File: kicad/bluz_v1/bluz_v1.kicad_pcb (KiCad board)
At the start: 2 copper layers, 24.9 x 14.9 mm, 61 parts, among them J1 USB_B_Micro, J10 Conn, J11 Conn, J12 BTAnt, J2 Conn, J3 Conn, J4 Conn, J5 Conn, J6 Conn, J7 Conn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

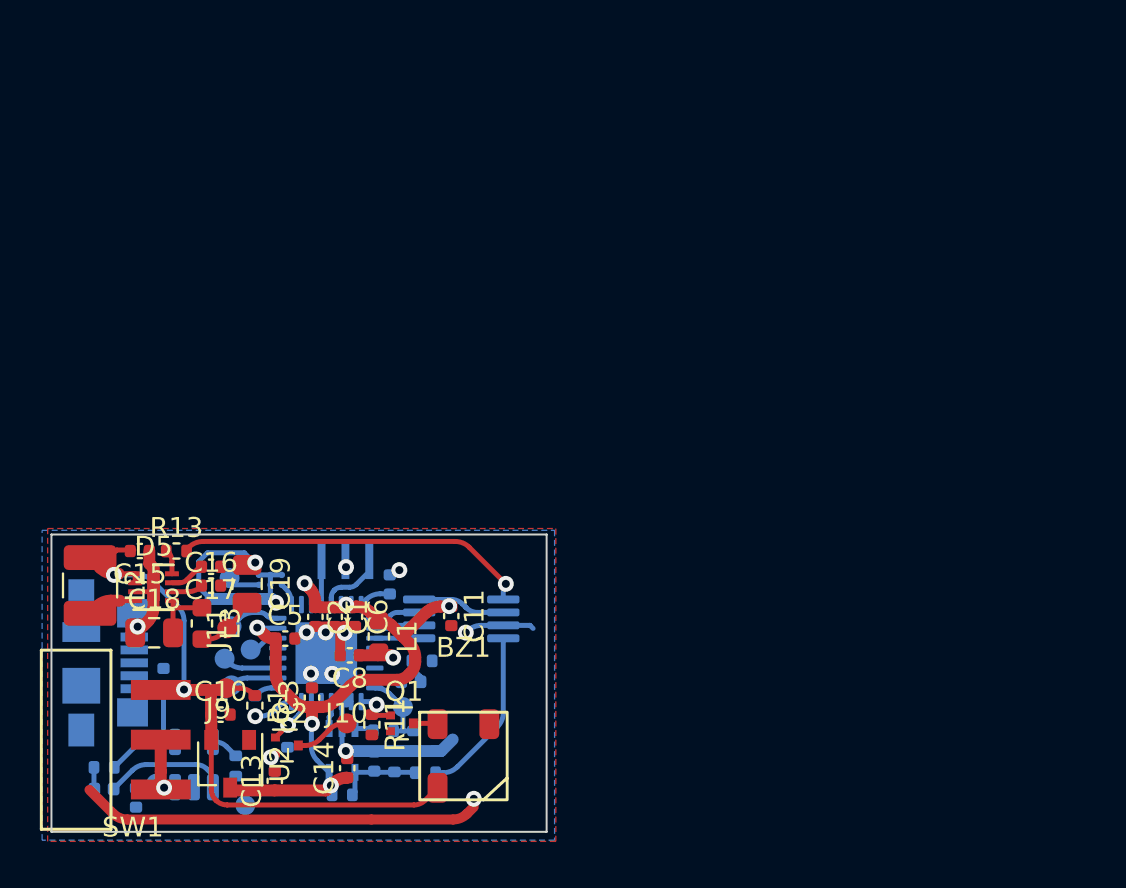
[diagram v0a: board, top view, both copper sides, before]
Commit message: удалено:       kicad/bluz_v1/bluz_v1-backups/bluz_v1-2024-05-03_143044.zip 	изменено:      kicad/bluz_v1/bluz_v1.kicad_pcb 	изменено:      kicad/bluz_v1/bluz_v1.kicad_prl 	изменено:      kicad/bluz_v1/bluz_v1.kicad_pro 	изменено:      kicad/bluz_v1/bluz_v1.kicad_sch
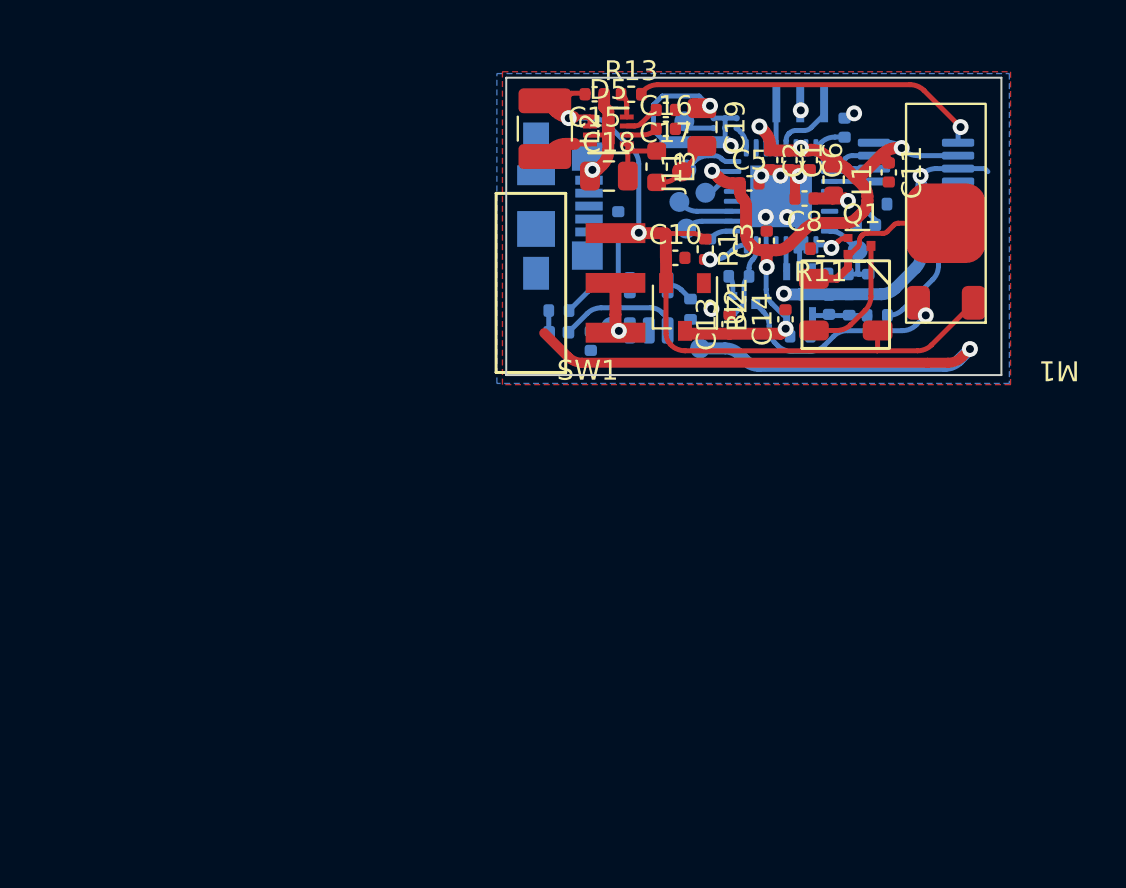
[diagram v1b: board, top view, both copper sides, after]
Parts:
- removed J10, J9: Conn, lib:conn_mini
- added M1: VibroMotor, MyLibrary:VibroMotor, F.Cu at (83.8, 48.4)
- Q2: moved to B.Cu
- U3: value TLV3201AIDBVT -> TLV3201AIDCK
- moved Q1 33.2 mm to (79.5, 45.6)
- moved R11 32.9 mm to (77.5, 45.7), turned to 180 degrees
- moved C5 32.7 mm to (73.9, 42.4)
- moved R9 32.6 mm to (76.5, 50.1)
- moved U3 32.5 mm to (76.4, 48.0)
- moved R12 32.4 mm to (73.4, 47.1), turned to 180 degrees
- moved L1 32.4 mm to (78.2, 42.2)
- moved R2 32.4 mm to (71.9, 45.7)
- moved C1 32.4 mm to (75.9, 41.2)
- moved C3 32.4 mm to (74.8, 45.3)
- moved J1 32.4 mm to (64.4, 43.6)
- moved J12 32.4 mm to (70.7, 39.3)
- moved L3 32.4 mm to (69.3, 41.6)
- moved R10 32.4 mm to (78.9, 48.5)
- moved C10 32.4 mm to (70.2, 46.2)
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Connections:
- BZ1 pad 3: (no net) -> GND
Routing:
- net GND: track 55.9 -> 85.4 mm
- net Net-(M1-Pad2): track 2.79 -> 11.4 mm, vias 0 -> 1
- net +BATT: track 34.3 -> 39.8 mm
- net Net-(BZ1-Pad1): track 1.47 -> 6.25 mm
- net Vibro: track 2.23 -> 3.85 mm, vias 1 -> 0
- net +2V8: track 41.3 -> 40.8 mm

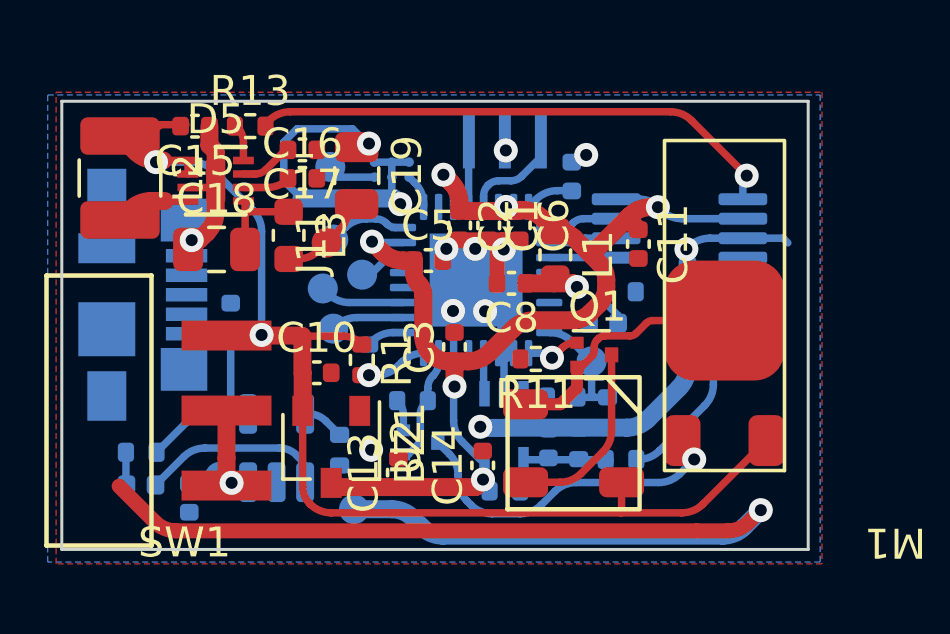
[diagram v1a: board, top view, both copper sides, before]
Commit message: новый файл:    Documents/NX2016AB-32MHZ ST2.pdf 	новый файл:    Documents/NX2016SA-2_e.pdf 	новый файл:    Documents/stm32wba-nucleo64-mb1863.pdf 	изменено:      kicad/bluz_v1/bluz_v1.kicad_pcb 	изменено:      kicad/bluz_v1/bluz_v1.kicad_sch
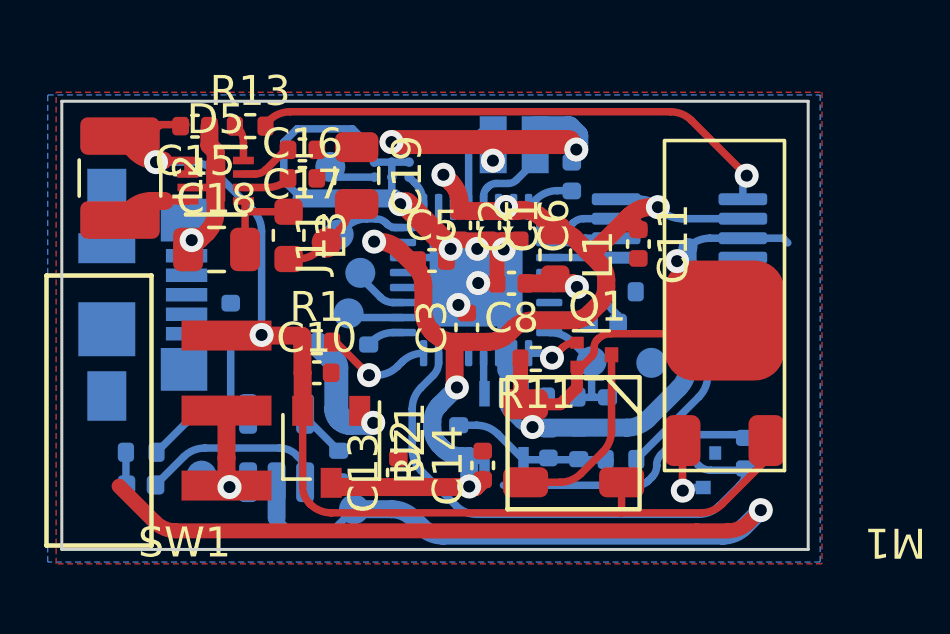
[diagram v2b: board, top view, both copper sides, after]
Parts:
- removed C9: C, Capacitor_SMD:C_0402_1005Metric
- Y1: value 16MHz -> NX2016SA-32MHz; footprint Crystal:Resonator_SMD_Murata_CSTxExxV-3Pin_3.0x1.1mm -> Crystal:Crystal_SMD_2016-4Pin_2.0x1.6mm
- moved R12 11.2 mm to (84.5, 48.8), turned to 90 degrees
- moved J3 10.1 mm to (81.3, 45.8)
- moved Q2 9.47 mm to (83.1, 49.4), turned to -90 degrees
- moved R9 2.28 mm to (74.9, 48.4), turned to 90 degrees
- moved R1 1.61 mm to (70.2, 45.1), turned to 0 degrees
- moved J4 1.35 mm to (71.7, 42.8)
- moved C3 0.77 mm to (75.2, 44.6)
- moved J5 0.72 mm to (71.3, 44.2)
- moved J6 0.61 mm to (66.4, 49.6)
- moved R3 0.53 mm to (70.9, 49.3)
- moved Y1 0.35 mm to (76.8, 38.6)
- moved J2 0.25 mm to (70.9, 41.5)
- moved C5 0.12 mm to (74.0, 42.4)
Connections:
- D1 pad 22: Net-(D1-Pad22) -> GND
- J3 pad 1: Net-(D1-Pad22) -> GND
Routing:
- net GND: track 85.4 -> 115.7 mm
- net Vibro: track 3.85 -> 18.6 mm
- net Net-(M1-Pad2): track 11.4 -> 3.05 mm
- net batLev: track 2.03 -> 3.71 mm
- net +BATT: track 39.8 -> 38.2 mm
- net Net-(D1-Pad22): track 1.58 -> 0.00 mm
- net Net-(C12-Pad1): track 4.04 -> 5.36 mm
- net Net-(D1-Pad19): track 2.82 -> 1.89 mm
- net +2V8: track 40.8 -> 41.7 mm
- net Net-(D1-Pad28): track 2.24 -> 3.08 mm
- net Net-(D1-Pad29): track 3.43 -> 2.60 mm
- net Net-(SW1-Pad2): track 4.81 -> 4.23 mm
- net Net-(D1-Pad18): track 2.43 -> 1.87 mm

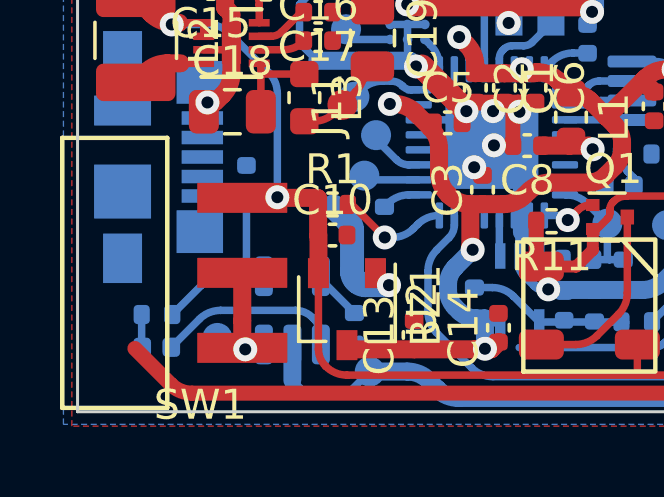
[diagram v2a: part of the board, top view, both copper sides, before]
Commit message: удалено:       kicad/bluz_v1/bluz_v1-backups/bluz_v1-2024-04-18_173246.zip 	удалено:       kicad/bluz_v1/bluz_v1-backups/bluz_v1-2024-04-18_175303.zip 	удалено:       kicad/bluz_v1/bluz_v1-backups/bluz_v1-2024-04-18_180313.zip 	изменено:      kicad/bluz_v1/bluz_v1.kicad_pcb 	изменено:      kicad/bluz_v1/bluz_v1.kicad_sch 	изменено:      kicad/bluz_v1/fp-info-cache
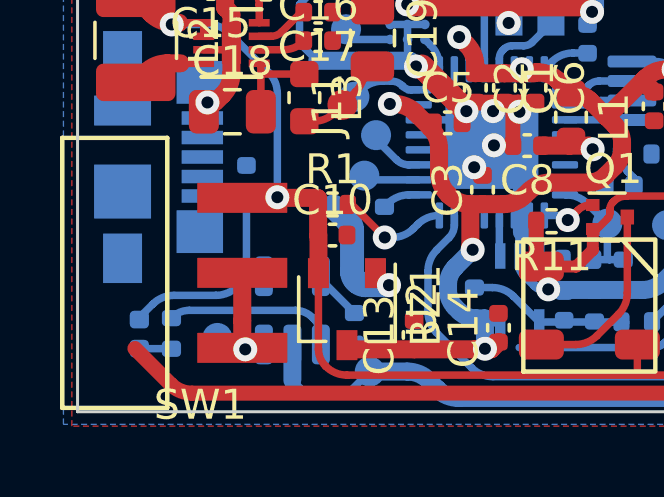
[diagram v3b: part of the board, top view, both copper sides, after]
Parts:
- moved R4 0.79 mm to (64.8, 49.4), turned to 90 degrees
- moved D2 0.73 mm to (63.8, 49.5), turned to 90 degrees
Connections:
- D2 pad 2: Net-(D2-Pad2) -> Net-(C4-Pad1)
- R4 pad 1: Net-(C4-Pad1) -> Net-(D2-Pad1)
- R4 pad 2: Net-(D2-Pad2) -> Net-(U1-Pad1)
- U1 pad 1: Net-(D2-Pad1) -> Net-(U1-Pad1)
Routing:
- net Net-(U1-Pad1): track 0.00 -> 5.81 mm
- net Net-(D2-Pad1): track 6.20 -> 1.07 mm
- net Net-(C4-Pad1): track 7.77 -> 8.93 mm
- net Net-(D2-Pad2): track 1.10 -> 0.00 mm

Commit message: новый файл:    Documents/NX2016SA-32M.pdf 	новый файл:    Documents/an2834-how-to-optimize-the-adc-accuracy-in-the-stm32-mcus-stmicroelectronics.pdf 	новый файл:    Documents/an5290-minimal-bom-for-stm32wb-series-microcontrollers-stmicroelectronics.pdf 	новый файл:    Documents/an5928-how-to-build-a-short-range-wireless-application-with-stm32wba-mcus-stmicroelectronics.pdf 	новый файл:    Documents/ndk_08142018_NX2016SA-32M-EXS00A-CS06465_SS-1389053.pdf 	удалено:       kicad/bluz_v1/bluz_v1-backups/bluz_v1-2024-04-18_181745.zip 	изменено:      kicad/bluz_v1/bluz_v1.kicad_pcb 	изменено:      kicad/bluz_v1/fp-info-cache
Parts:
- moved R12 1.15 mm to (84.7, 50.0), turned to -90 degrees
- moved Q2 0.80 mm to (83.2, 50.2), turned to 180 degrees
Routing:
- net Vibro: track 18.6 -> 16.6 mm
- net Net-(M1-Pad2): track 3.05 -> 2.47 mm

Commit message: изменено:      kicad/bluz_v1/bluz_v1.kicad_pcb 	изменено:      kicad/bluz_v1/bluz_v1.kicad_prl 	изменено:      kicad/bluz_v1/bluz_v1.kicad_sch
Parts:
- U2: value MCP1703 -> MCP1700; footprint Package_TO_SOT_SMD:SOT-23W -> Package_TO_SOT_SMD:SOT-23
- moved R1 1.49 mm to (71.2, 46.2)
- moved C10 1.34 mm to (71.2, 45.2)
- moved J7 0.95 mm to (72.2, 50.2)
- moved C13 0.30 mm to (73.2, 49.6)
- moved U2 0.06 mm to (70.7, 48.7), turned to 90 degrees
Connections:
- U2 pad 2: +BATT -> +2V8
- U2 pad 3: +2V8 -> +BATT
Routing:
- net GND: track 116.0 -> 118.1 mm, vias 14 -> 16
- net batLev: track 3.71 -> 2.03 mm
- net +BATT: track 38.2 -> 36.7 mm
- net +2V8: track 41.7 -> 40.6 mm

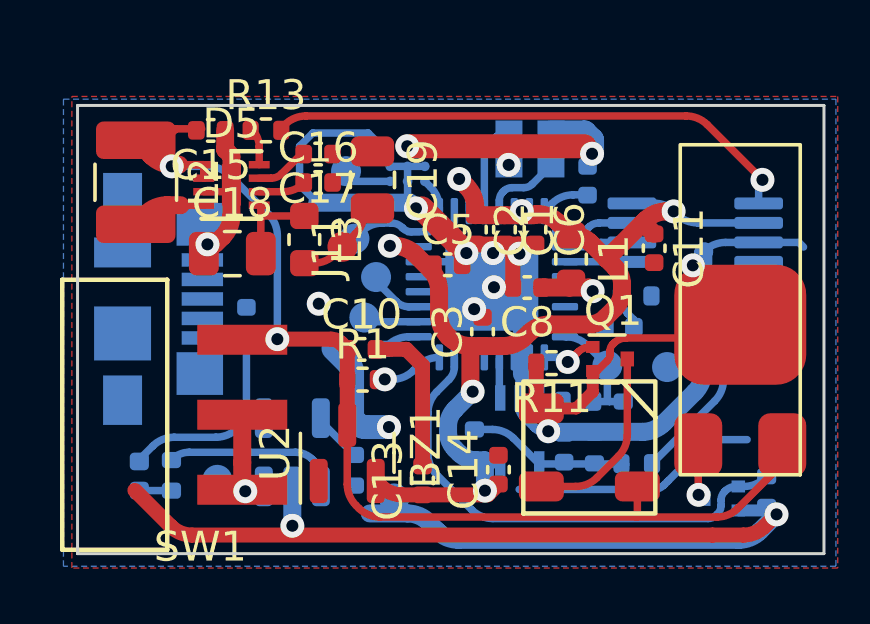
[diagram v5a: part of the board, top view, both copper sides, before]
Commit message: удалено:       kicad/bluz_v1/bluz_v1-backups/bluz_v1-2024-04-18_190147.zip 	удалено:       kicad/bluz_v1/bluz_v1-backups/bluz_v1-2024-04-19_183106.zip 	удалено:       kicad/bluz_v1/bluz_v1-backups/bluz_v1-2024-04-19_183722.zip 	удалено:       kicad/bluz_v1/bluz_v1-backups/bluz_v1-2024-04-19_184242.zip 	удалено:       kicad/bluz_v1/bluz_v1-backups/bluz_v1-2024-04-19_185221.zip 	изменено:      kicad/bluz_v1/bluz_v1.kicad_pcb 	изменено:      kicad/bluz_v1/bluz_v1.kicad_prl 	изменено:      kicad/bluz_v1/bluz_v1.kicad_sch 	изменено:      kicad/bluz_v1/fp-info-cache 	Documents/rm0493-multiprotocol-wireless-bluetooth-lowenergy-and-ieee802154-stm32wba5xxx-armbased-32bit-mcus-stmicroelectronics.pdf 	Documents/tn1163-description-of-wlcsp-for-microcontrollers-and-recommendations-for-its-use-stmicroelectronics.pdf
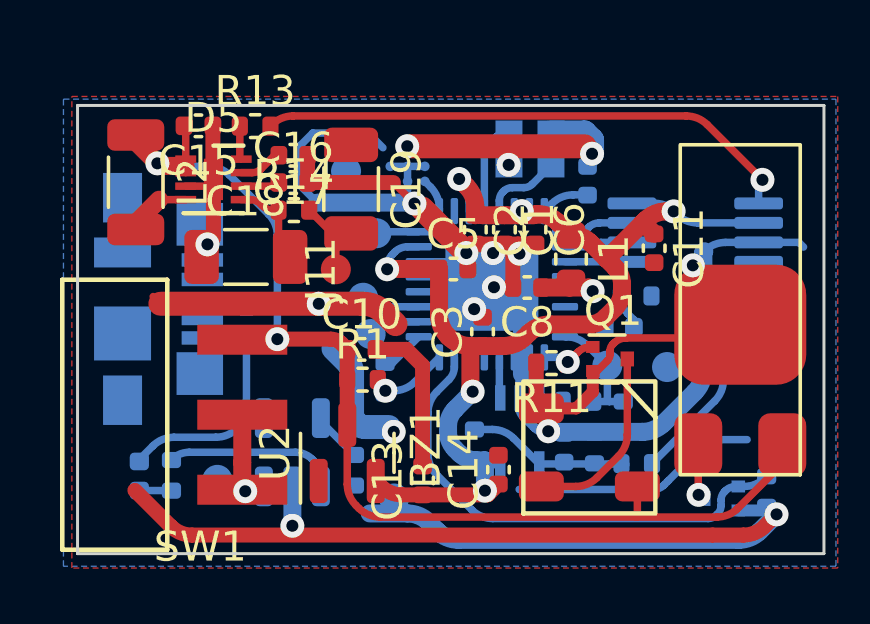
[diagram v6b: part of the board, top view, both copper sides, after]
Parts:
- removed L3: 47uH, Inductor_SMD:L_0603_1608Metric
- added R14: 470, Resistor_SMD:R_0402_1005Metric, F.Cu at (68.9, 40.6)
- C15: value C -> 10u
- C16, C17: value C -> .47
- C18, C19: value C -> 10u; footprint Capacitor_SMD:C_0805_2012Metric -> Capacitor_SMD:C_1206_3216Metric
- L2: value 47uH -> 560uH; footprint Inductor_SMD:L_1210_3225Metric -> Inductor_SMD:L_1206_3216Metric
- moved C17 0.83 mm to (68.9, 38.8)
- moved C16 0.83 mm to (68.9, 39.7)
- moved J4 0.81 mm to (71.2, 43.5)
- moved J11 0.78 mm to (70.3, 42.6)
- moved C19 0.77 mm to (70.8, 39.9)
- moved J2 0.75 mm to (71.7, 41.4)
- moved D5 0.63 mm to (66.2, 39.6)
- moved J5 0.59 mm to (71.5, 44.7)
- moved R2 0.47 mm to (72.0, 46.2)
- moved C18 0.46 mm to (67.3, 42.2)
- moved C15 0.44 mm to (65.7, 37.8)
- moved R13 0.39 mm to (67.6, 37.8)
- moved C5 0.24 mm to (74.2, 42.6)
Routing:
- net GND: track 118.1 -> 131.2 mm
- net Net-(D1-Pad24): track 2.39 -> 1.43 mm
- net +2V8: track 40.6 -> 41.2 mm

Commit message: удалено:       kicad/bluz_v1/bluz_v1-backups/bluz_v1-2024-04-19_190122.zip 	удалено:       kicad/bluz_v1/bluz_v1-backups/bluz_v1-2024-04-22_153028.zip 	удалено:       kicad/bluz_v1/bluz_v1-backups/bluz_v1-2024-04-26_142701.zip 	удалено:       kicad/bluz_v1/bluz_v1-backups/bluz_v1-2024-05-03_144119.zip 	удалено:       kicad/bluz_v1/bluz_v1-backups/bluz_v1-2024-05-03_145331.zip 	изменено:      kicad/bluz_v1/bluz_v1.kicad_pcb 	изменено:      kicad/bluz_v1/bluz_v1.kicad_sch 	изменено:      kicad/bluz_v1/fp-info-cache
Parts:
- removed C17: .47, Capacitor_SMD:C_0402_1005Metric
- removed C18: 10u, Capacitor_SMD:C_1206_3216Metric
- added C9: 1.5p, Capacitor_SMD:C_0402_1005Metric, F.Cu at (66.8, 38.1)
- added R15: 4.3M, Resistor_SMD:R_0402_1005Metric, F.Cu at (67.7, 38.5)
- added R16: 100M, Resistor_SMD:R_0603_1608Metric, F.Cu at (65.1, 38.7)
- added U4: AP3015KTR, Package_TO_SOT_SMD:SOT-23-5, F.Cu at (67.5, 41.1)
- BZ1: footprint lib:Buzzer5x5 -> MyLibrary:Buzzer55x55
- C10, C14, C15: moved to B.Cu
- C16: value .47 -> 10u; footprint Capacitor_SMD:C_0402_1005Metric -> Capacitor_SMD:C_0805_2012Metric
- C19: footprint Capacitor_SMD:C_1206_3216Metric -> Capacitor_SMD:C_0805_2012Metric
- D5: value LT8410 -> BAT46JFILM; footprint Package_DFN_QFN:DFN-8-1EP_2x2mm_P0.45mm_EP0.64x1.38mm -> Diode_SMD:D_SOD-323
- L2: value 560uH -> 220uH
- R13: value R -> 100M
- U2: footprint Package_TO_SOT_SMD:SOT-23 -> Package_TO_SOT_SMD:SOT-23-3
- moved J11 9.14 mm to (62.5, 37.9)
- moved C19 8.00 mm to (62.9, 41.1), turned to 90 degrees
- moved L2 6.85 mm to (70.3, 41.1), turned to 90 degrees
- moved R13 6.81 mm to (74.4, 37.7)
- moved Q1 6.38 mm to (74.6, 49.7)
- moved R14 6.22 mm to (62.9, 38.9), turned to 180 degrees
- moved C15 4.88 mm to (67.8, 42.2), turned to 0 degrees
- moved R11 4.34 mm to (73.8, 48.0), turned to 90 degrees
- moved C13 4.28 mm to (73.9, 45.4), turned to -90 degrees
- moved D5 4.20 mm to (70.2, 38.1)
- moved C16 4.19 mm to (65.0, 41.1), turned to 90 degrees
- moved U2 3.70 mm to (71.5, 45.1), turned to 180 degrees
- moved R3 3.31 mm to (70.2, 46.0), turned to 0 degrees
- moved C10 2.36 mm to (68.8, 44.9)
- moved R9 2.25 mm to (76.5, 50.0), turned to 0 degrees
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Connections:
- C16 pad 1: Net-(C16-Pad1) -> GND
- C16 pad 2: GND -> Net-(C16-Pad2)
- D5 pad 1: +BATT -> Net-(C16-Pad2)
- D5 pad 2: +BATT -> Net-(D5-Pad2)
- L2 pad 2: Net-(D5-Pad4) -> Net-(D5-Pad2)
- R13 pad 1: Net-(D5-Pad8) -> Net-(C9-Pad2)
- R14 pad 1: Net-(C18-Pad2) -> Net-(C16-Pad2)
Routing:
- net GND: track 131.2 -> 153.9 mm, vias 16 -> 15
- net Net-(C9-Pad2): track 0.00 -> 10.5 mm
- net Net-(C16-Pad2): track 0.00 -> 8.16 mm
- net HVAdj: track 18.2 -> 11.3 mm
- net Sound: track 1.90 -> 7.63 mm
- net +BATT: track 36.3 -> 31.1 mm
- net Net-(BZ1-Pad1): track 6.25 -> 1.63 mm
- net Net-(D5-Pad2): track 0.00 -> 3.74 mm
- net +2V8: track 41.2 -> 37.7 mm, vias 6 -> 5
- net Net-(C18-Pad2): track 3.06 -> 0.00 mm
- net Net-(D5-Pad4): track 2.20 -> 0.00 mm
- net Net-(C12-Pad1): track 5.36 -> 3.80 mm
- net Net-(C17-Pad2): track 1.48 -> 0.00 mm
- net Net-(C16-Pad1): track 1.30 -> 0.00 mm
- net Net-(D5-Pad8): track 1.12 -> 0.00 mm
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
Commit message: изменено:      kicad/bluz_v1/bluz_v1.kicad_pcb 	изменено:      kicad/bluz_v1/bluz_v1.kicad_prl 	изменено:      kicad/bluz_v1/bluz_v1.kicad_sch
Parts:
- moved R13 5.64 mm to (68.8, 38.4)
- moved D5 1.20 mm to (71.4, 38.1)
- moved R14 0.81 mm to (63.3, 38.2), turned to 90 degrees
- moved C15 0.62 mm to (67.8, 42.8)
- moved U4 0.42 mm to (67.6, 41.5)
- moved R15 0.40 mm to (67.7, 38.9)
- moved BZ1 0.29 mm to (78.4, 48.1)
- moved C9 0.28 mm to (66.8, 38.4)
- moved R16 0.18 mm to (65.0, 38.8)
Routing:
- net Net-(C9-Pad2): track 10.5 -> 4.35 mm
- net HVAdj: track 11.3 -> 17.4 mm
- net GND: track 153.9 -> 156.3 mm, vias 15 -> 16
- net Net-(C16-Pad2): track 8.16 -> 9.25 mm
- net /+SiPM: track 2.44 -> 3.38 mm
- net +2V8: track 37.7 -> 38.6 mm
- net +BATT: track 31.1 -> 30.2 mm
- net Net-(D5-Pad2): track 3.74 -> 4.61 mm
